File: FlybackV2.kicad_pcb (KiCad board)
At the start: 2 copper layers, 205.7 x 77.7 mm, 75 parts, among them J1 Power, J2 Divisor, J3 Conn_01x03, J4 Coils, Q6 2N3906, T2 0399-T208, U1 LT8304, U9 MAX4239

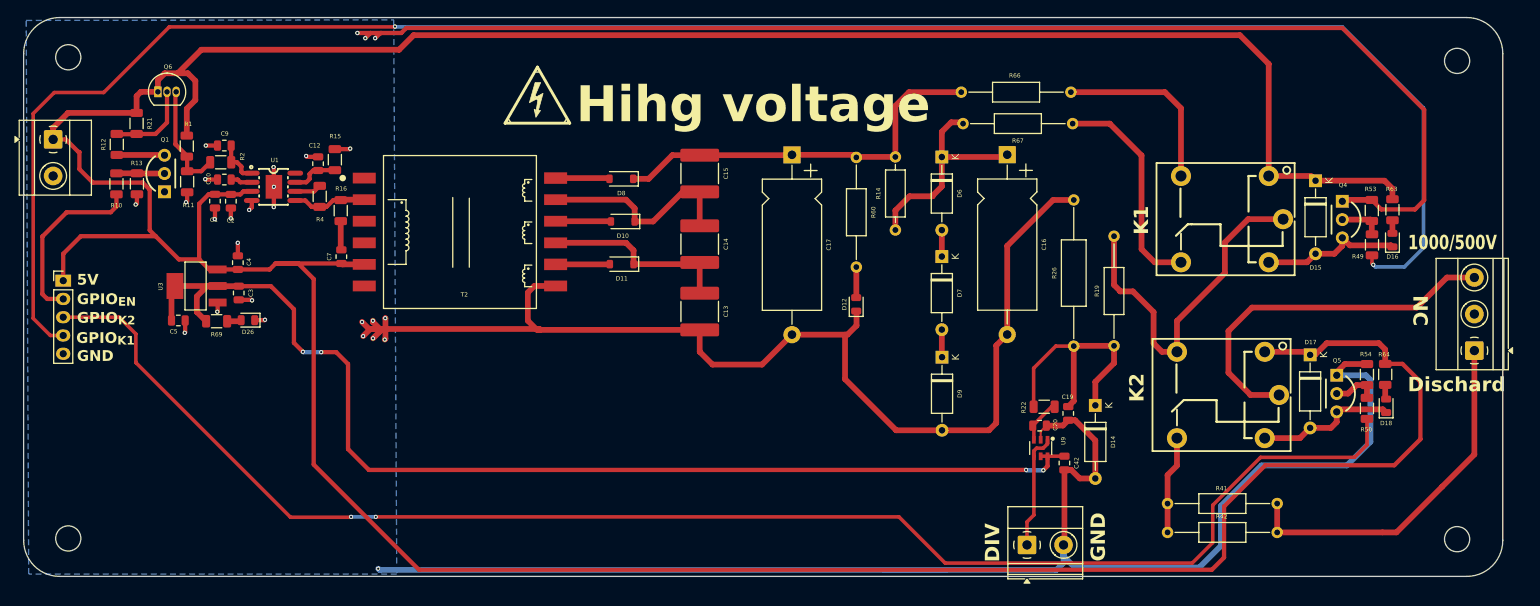
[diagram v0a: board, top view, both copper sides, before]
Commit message: now has a C for the 12V source
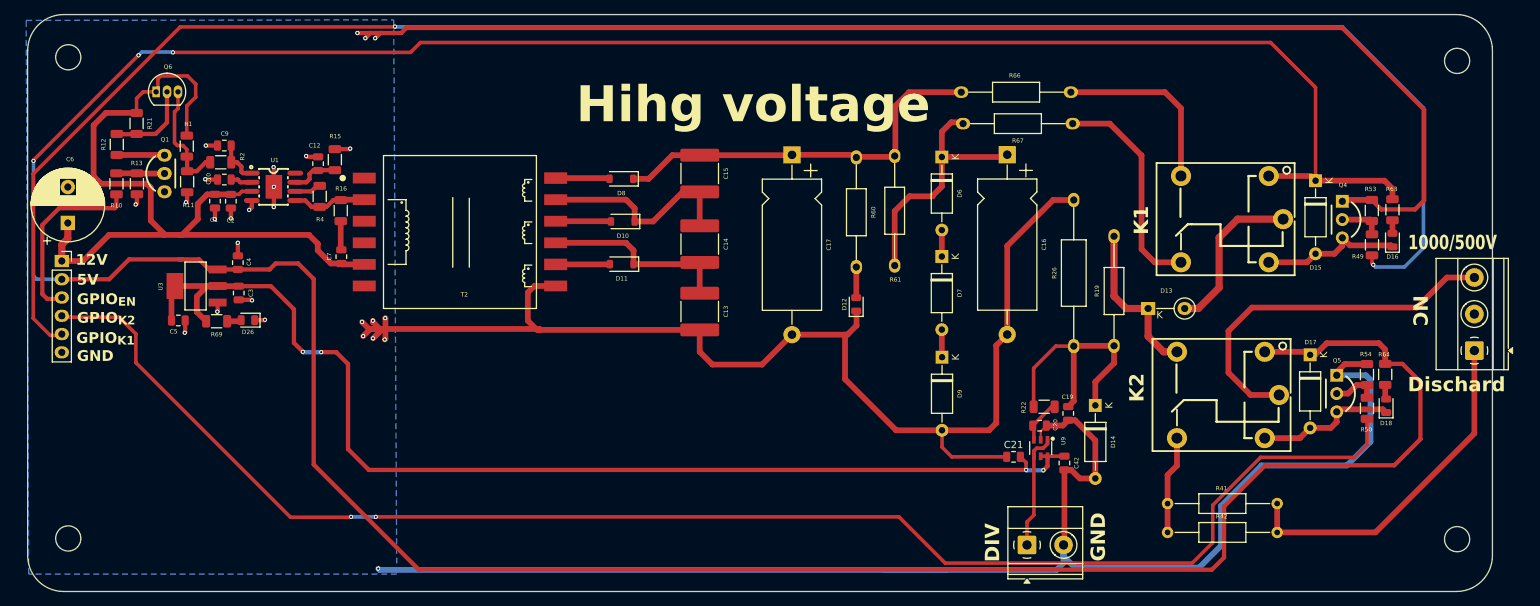
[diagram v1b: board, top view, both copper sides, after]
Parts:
- removed J4: Coils, Connector_PinHeader_2.54mm:PinHeader_1x05_P2.54mm_Vertical
- removed R14: 2M, Resistor_THT:R_Axial_DIN0207_L6.3mm_D2.5mm_P10.16mm_Horizontal
- removed REF**: Symbol_HighVoltage_Triangle_6x6mm_Copper, Symbol:Symbol_HighVoltage_Triangle_6x6mm_Copper
- added C21: 0.1uF, Capacitor_SMD:C_0805_2012Metric, F.Cu at (181.5, 117.0)
- added C6: 1000uF, Capacitor_THT:CP_Radial_D10.0mm_P5.00mm, F.Cu at (50.0, 84.5)
- added D13: 100V, Diode_THT:D_A-405_P5.08mm_Vertical_KathodeUp, F.Cu at (200.2, 96.4)
- added R61: 470K, Resistor_THT:R_Axial_DIN0207_L6.3mm_D2.5mm_P15.24mm_Horizontal, F.Cu at (165.0, 90.4)
- J1: value Power -> Conn_01x06; footprint TerminalBlock_Phoenix:TerminalBlock_Phoenix_MKDS-1,5-2-5.08_1x02_P5.08mm_Horizontal -> Connector_PinSocket_2.54mm:PinSocket_1x06_P2.54mm_Vertical
- R1: value 10K -> 100K
- R66: value 2M -> 1M
- R67: value 2M -> 470K
- moved J1 16.9 mm to (49.2, 89.8), turned to 0 degrees
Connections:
- C1 pad 1: +5V -> 12V
- C2 pad 1: +5V -> 12V
- C7 pad 1: +5V -> 12V
- J1 pad 1: +5V -> 12V
- J1 pad 2: GND -> +5V
- Q6 pad 1: +5V -> 12V
- R1 pad 1: +5V -> 12V
- R19 pad 2: Net-(R19-Pad2) -> Net-(D13-K)
- R21 pad 1: +5V -> 12V
- R32 pad 5: Net-(R19-Pad2) -> Net-(D13-A)
- R33 pad 2: Net-(R19-Pad2) -> Net-(D13-K)
- T2 pad 5: +5V -> 12V
- U1 pad 3: +5V -> 12V
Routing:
- net 12V: track 0.00 -> 115.8 mm
- net Net-(R19-Pad2): track 49.4 -> 0.00 mm
- net +5V: track 552.6 -> 510.0 mm, vias 0 -> 3
- net Net-(D13-A): track 0.00 -> 22.9 mm
- net Net-(D13-K): track 0.00 -> 22.6 mm
- net GND: track 585.8 -> 597.7 mm
- net 500V: track 31.0 -> 36.0 mm
- net /GPIO_{K1}: track 265.7 -> 260.8 mm
- net +3.3_{iso}V: track 159.0 -> 161.1 mm
- net Net-(J3-Pin_1): track 50.4 -> 48.6 mm
- net /GPIO_{EN}: track 24.9 -> 25.8 mm
- net Net-(Q6-C): track 15.5 -> 16.1 mm
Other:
- board size 205.7 x 77.7 mm -> 203.7 x 80.2 mm
- board text added: "12V"

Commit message: update: it versin goes to production
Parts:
- C6: footprint Capacitor_THT:CP_Radial_D10.0mm_P5.00mm -> Capacitor_THT:CP_Radial_D13.0mm_P5.00mm
- J1: footprint Connector_PinSocket_2.54mm:PinSocket_1x06_P2.54mm_Vertical -> Connector_PinHeader_2.54mm:PinHeader_1x06_P2.54mm_Vertical
- R11: value 10K -> 1K
- R2: value 1K -> 0
- R26: footprint Resistor_THT:R_Axial_DIN0309_L9.0mm_D3.2mm_P20.32mm_Horizontal -> Resistor_THT:R_Axial_DIN0207_L6.3mm_D2.5mm_P15.24mm_Horizontal
- moved C6 31.5 mm to (76.3, 67.1), turned to 0 degrees
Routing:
- net GND: track 597.7 -> 491.8 mm, vias 27 -> 26
- net 12V: track 115.8 -> 122.5 mm
- net Net-(D14-K): track 35.9 -> 38.9 mm
- net Net-(R32-Pad3): track 30.7 -> 29.6 mm
- net /GPIO_{K2}: track 211.3 -> 212.2 mm
- net +5V: track 510.0 -> 509.4 mm

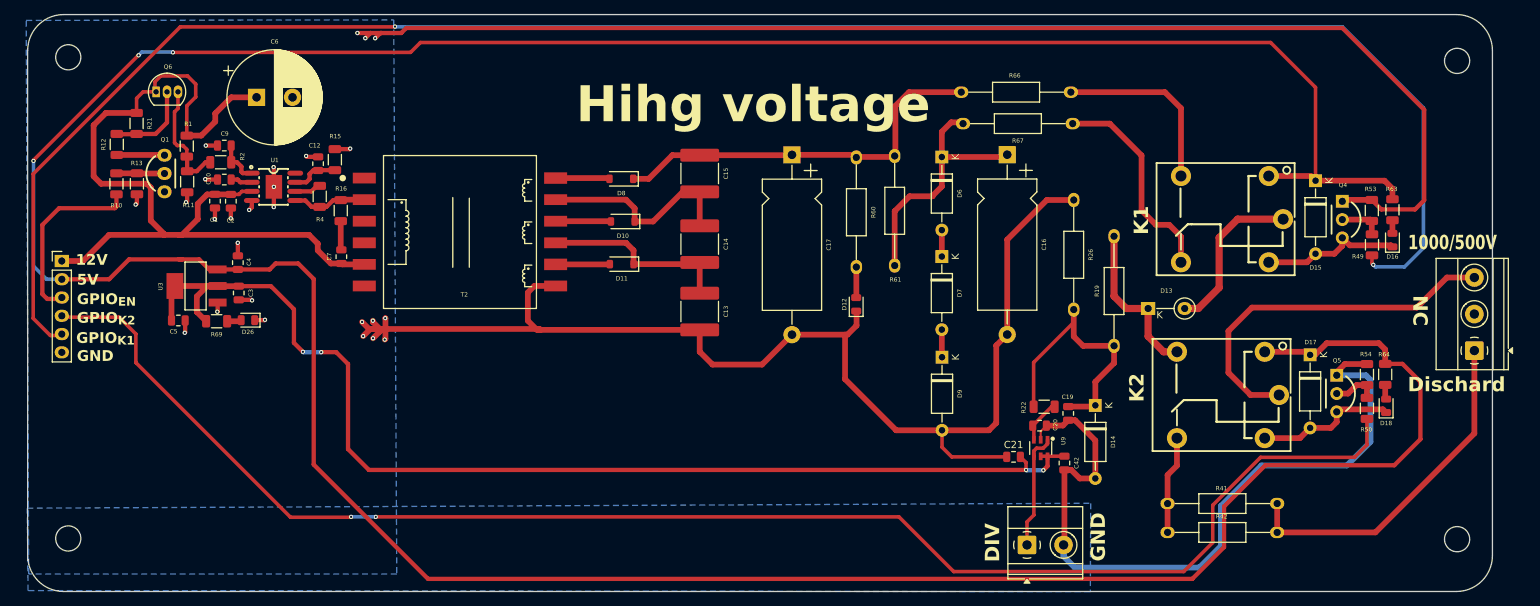
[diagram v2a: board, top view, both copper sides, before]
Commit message: uptade: jlcs part number
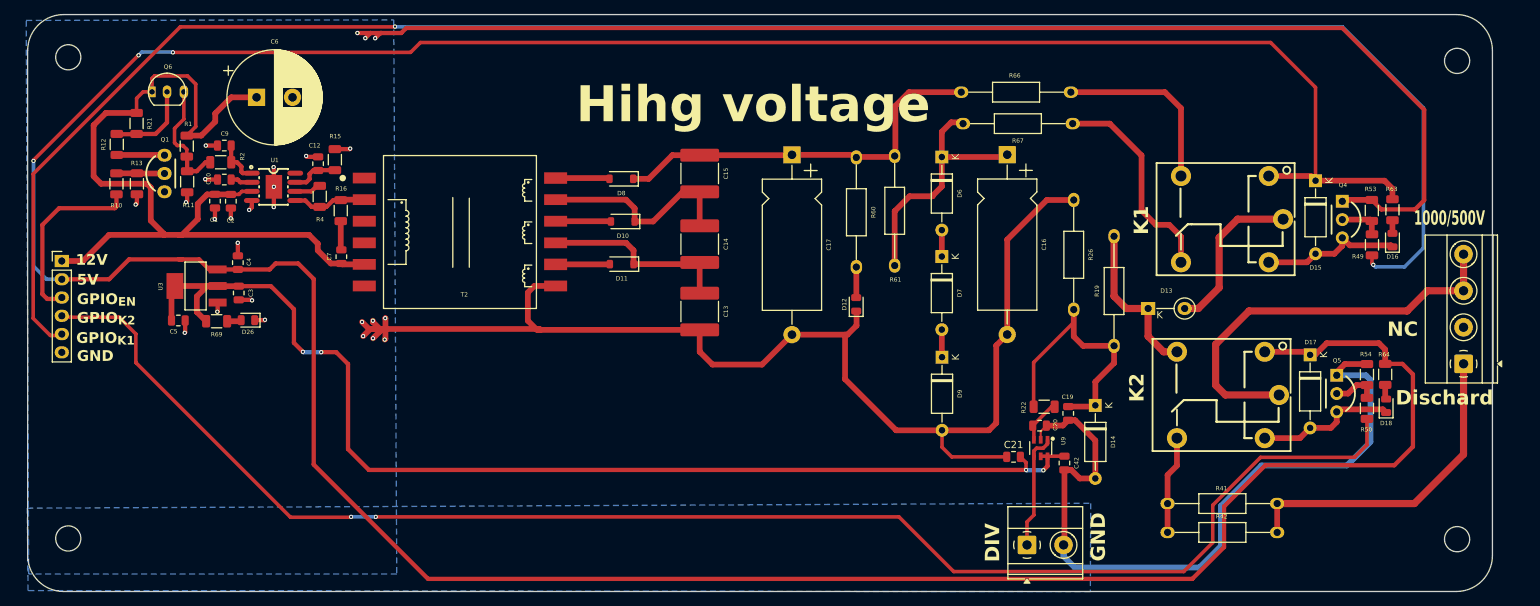
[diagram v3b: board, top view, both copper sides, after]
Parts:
- removed J3: Conn_01x03, TerminalBlock_Phoenix:TerminalBlock_Phoenix_MKDS-1,5-3-5.08_1x03_P5.08mm_Horizontal
- added J4: 1000/500V out, TerminalBlock_Phoenix:TerminalBlock_Phoenix_MKDS-1,5-4-5.08_1x04_P5.08mm_Horizontal, F.Cu at (244.1, 104.1)
- C13, C14, C15: value 0.22u -> 0.22uF
- C16, C17, C19, C20: value 1u -> 1uF
- C3: value 0.1u -> 0.1uF
- C4, C42, C5: value 10u -> 10uF
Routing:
- net Net-(J4-Pin_3): track 51.4 -> 57.7 mm
- net Net-(J4-Pin_1): track 48.6 -> 45.3 mm
- net +5V: track 509.4 -> 508.5 mm
